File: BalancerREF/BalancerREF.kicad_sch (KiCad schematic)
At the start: 81 parts, among them J1 USB4105-GF-A, J2 LiPo 500mAh PROTECTED, J3 MAG+ / MAG- PTH, J4 GPS MODULE 3V3 UART, J5 OPTICAL HEAD 7-WAY, Q3 AO3401A, Q4 AO3401A, SW1 POWER, SW2 ACQUIRE, SW3 BOOT / SERVICE, U1 ESP32-S3-MINI-1-N8, U10 SN74LVC1G123DCTR, U2 IIS3DWBTR, U3 LM1815MX/NOPB, U5 MCP73831T-2ACI/OT, U6 TPS63031DSKR, U7 SRV05-4MR6T1G, U9 SN74LVC1G08DBVR

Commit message: feat: BQ24075 charge management, drop BAT_SENSE, sweep wire stubs
Replaces the MCP73831 + D2 + Q3 + R27 + R31 discrete charger and power-path
with a BQ24075RGT, which does the same job with an integrated DPPM path and
adds what the discrete version could not: independent system/charge supply,
operation with a defective or absent cell, USB-IF inrush limiting, and VIN-DPM
so a weak port sags instead of collapsing.

New support parts: R3 3.57k ISET (~249 mA, about 0.5C), R35 1.6k ILIM (~1.0 A),
R36 10k on TS for the absent pack thermistor, R37/R38 100k pull-ups, C30 10uF
on OUT. CE and SYSOFF tied low; TMR left open for the default safety timers.
EN1/EN2/PGOOD/CHG go to GPIO5/18/21/38.

BAT_SENSE (R33/R34/C31 on GPIO4) is removed. It existed only to infer USB
presence by comparing SYS_SW against BAT; PGOOD reports a valid input source
directly, so the inference is redundant. That also retires a 500k ADC source
impedance and a ~2uA standing drain on the cell.

Every BQ24075 pin is verified against SLUS810N Rev N, now saved in sources/.
Two things that check surfaced:
  - SYS sits ~0.4 V higher without D2's drop. Still inside the TPS63031's
    1.8-5.5 V recommended range, and the failure mode improved: OUT clamps at
    5.5 V and the input OVPs at 6.6 V, where the diode passed everything
    through. Wants a bench measurement with a 5.25 V source.
  - SUPPLY_SENSE is now the only supply measurement and it is on ADC2, the
    unit shared with the radio. That is why BAT_SENSE had been on ADC1.

Also in this change:
  - /SYS added to the Power net class. It is the BQ24075's OUT rail and
    carries the whole system load; at the 0.20 mm default it was rated 0.74 A.
    Dropped the dead Net-(D2-K) pattern.
  - Swept 19 dangling wire stubs plus an orphaned no-connect left by the
    optical split, SW4, R5 and this swap: 23 wires removed, 2 trimmed back to
    the label they carry. ERC goes from 20 warnings to 0.
  - Mounting holes pulled 0.25 mm inward so they clear U1's ante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
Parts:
- removed C31: 100n, Capacitor_SMD:C_0805_2012Metric, symbol Device:C
- removed D2: PMEG4010CEH, Diode_SMD:D_SOD-123F, symbol Device:D_Schottky
- removed Q3: AO3401A, Package_TO_SOT_SMD:SOT-23, symbol Transistor_FET:AO3401A
- removed R31: 1k, Resistor_SMD:R_0603_1608Metric, symbol Device:R
- removed R33, R34: 1M, Resistor_SMD:R_0603_1608Metric, symbol Device:R
- removed U5: MCP73831T-2ACI/OT, Package_TO_SOT_SMD:SOT-23-5, symbol Battery_Management:MCP73831-2-OT
- added R35: 1.6k, Resistor_SMD:R_0603_1608Metric, symbol Device:R
- added R36: 10k, Resistor_SMD:R_0603_1608Metric, symbol Device:R
- added R37, R38: 100k, Resistor_SMD:R_0603_1608Metric, symbol Device:R
- added U5: BQ24075RGT, Package_DFN_QFN:QFN-16-1EP_3x3mm_P0.5mm_EP1.675x1.675mm, symbol BalancerREF:BQ24075RGT
- R3: value 4.02k 1% -> 3.57k 1%; MPN 4.02k 1% -> 100k
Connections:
- net +3V3: now also R37.1, R38.1
- net BAT: now also U5.2 (BAT), U5.3 (BAT)
- net GND: now also R35.2, R36.2, U5.15 (SYSOFF), U5.17 (EP), U5.4 (~{CE}), U5.8 (VSS)
- net USB_VBUS: now also U5.13 (IN)
- net SYS: now reaches C30.1, SW1.1 (A)
- net SYS: now also U5.10 (OUT), U5.11 (OUT)
- net CHG_EN2: now reaches U1.22 (IO18)
- net CHG_EN2: now also U5.5 (EN2)
- net PGOOD_N: now reaches U1.25 (IO21)
- net PGOOD_N: now also R37.2, U5.7 (~{PGOOD})
- net CHG_STAT: now reaches U1.34 (IO38)
- net CHG_STAT: now also R38.2, U5.9 (~{CHG})
- net CHG_EN1: now reaches U1.9 (IO5)
- net CHG_EN1: now also U5.6 (EN1)
- net ISET: now reaches R3.1
- net ISET: now also U5.16 (ISET)
- net BAT_SENSE: no longer names the net of U1.8 (IO4)
- new net ILIM: R35.1, U5.12 (ILIM)
- new net TS: R36.1, U5.1 (TS)
- no-connect marks 35 -> 32

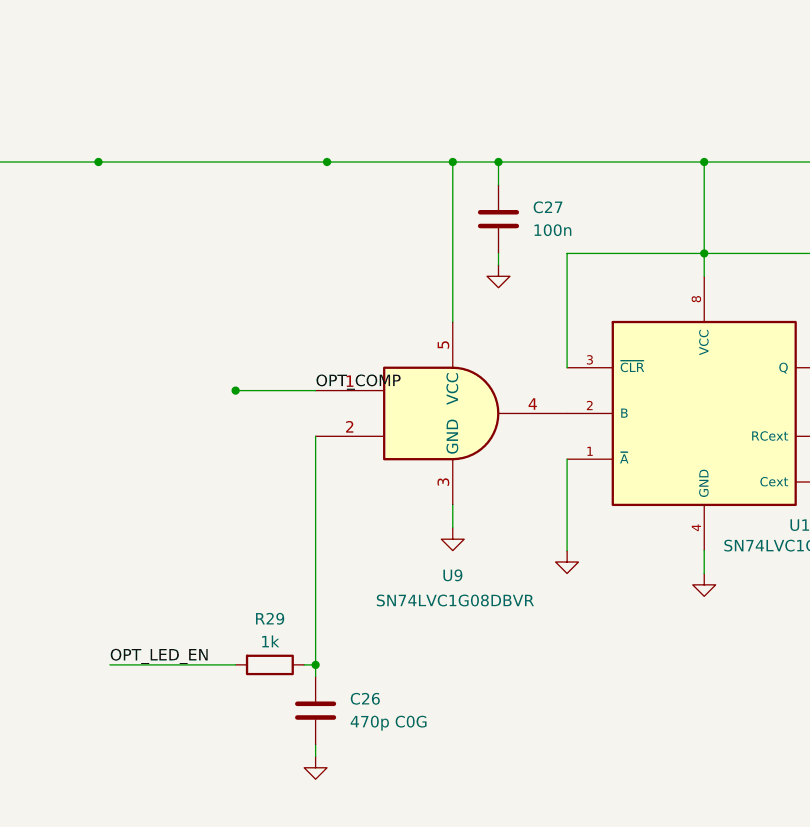
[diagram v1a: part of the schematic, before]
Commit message: fix: address repo review findings before routing
An external review raised seven pre-routing items plus smaller notes. Each was
checked against the manufacturer source rather than taken on faith; two did not
survive that check and are recorded as not-confirmed.

Confirmed and fixed:

  * D1 peak current. The head runs from SYS_SW, and with the BQ24075 regulating
    OUT to 5.5 V, R18 at 3.0 ohm gave ~1.1 A peak against D1's 1 A absolute
    maximum. The BOM note had only checked the 4.2 V battery case, and the
    charger swap - which replaced a Schottky holding SYS near 4.55 V - is what
    pushed it over. R18 -> 3.9 ohm: ~0.49 A at a full cell (the bench-set design
    point) and ~0.90 A worst case at 5.5 V with a low-Vf bin.
  * Charger stuck at USB100. EN1/EN2 have 285k internal pulldowns and nothing
    drove them, so the input limit covered system load AND charge current at
    100 mA. setupCharger() now selects USB500 at boot, and status reports
    input_present/charging from PGOOD and CHG.
  * U9 input transition rate. R29/C26 fed the SN74LVC1G08 a 0.47 us edge against
    a 10 ns/V spec, ~25x out. Swapped to SN74LVC1G132, a Schmitt NAND with the
    identical SOT-23-5 pinout (verified against SLVS322 Figure 4-1), which
    conditions both inputs. It inverts, so U10's trigger moved from B rising to
    ~A falling - the SN74LVC1G123 supports both edges.
  * Switcher parts on the wrong face. L1 and C4-C7 were on the back with U6 on
    the front, putting vias in a 2.4 MHz switching loop. Moved to the front;
    C2/C3/C30 followed for the BQ24075. The "ICs front, passives back" rule does
    not survive contact with a switching converter.
  * U1 decoupling. C8 is now 0.38 mm from the 3V3 pad instead of ~9 mm. Both
    stay on the back, since U1's body owns that part of the front.
  * Head board emitter loop, was spanning the full board width. C20/R18/Q1 now
    cluster in 6.9 x 3.3 mm. R21/C21 went from 4 mm off Q1 to 16 mm and sit
    3.6/3.9 mm from U8 pins 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
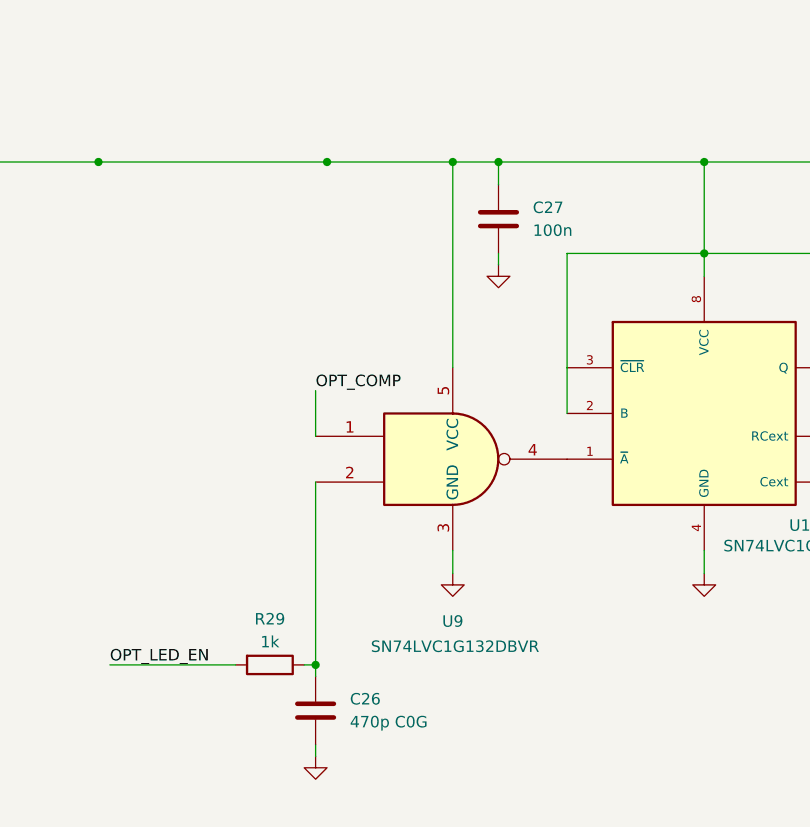
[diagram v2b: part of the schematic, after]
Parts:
- U9: value SN74LVC1G08DBVR -> SN74LVC1G132DBVR; symbol 74xGxx:74LVC1G08 -> BalancerREF:SN74LVC1G132
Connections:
- net +3V3: now also U10.2 (B)
- net GND: no longer U10.1 (~{A})
- net at U9.4: now also U10.1 (~{A}); no longer U10.2 (B)
